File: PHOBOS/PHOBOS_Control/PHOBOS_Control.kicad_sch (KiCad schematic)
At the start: 80 parts, among them J1 Screw_Terminal_01x02, J2 Conn_01x06, J3 Conn_Coaxial, J5 DE9_Pins_MountingHoles, J6 USB4056-03-A_REVA2, SW4 KMR211GLFS, U1 SX1280IMLTRT, U2 TLV9351IDCKR, U3 W25Q128JVSIQ, U4 NCP1117-3.3_SOT223, U5 RP2040, U6 TLV9351IDCKR, U7 TLV9351IDCKR, U8 TLV9351IDCKR, Y1 ABM8-272-T3, Y2 C1E-52.000-10-1012-X-M

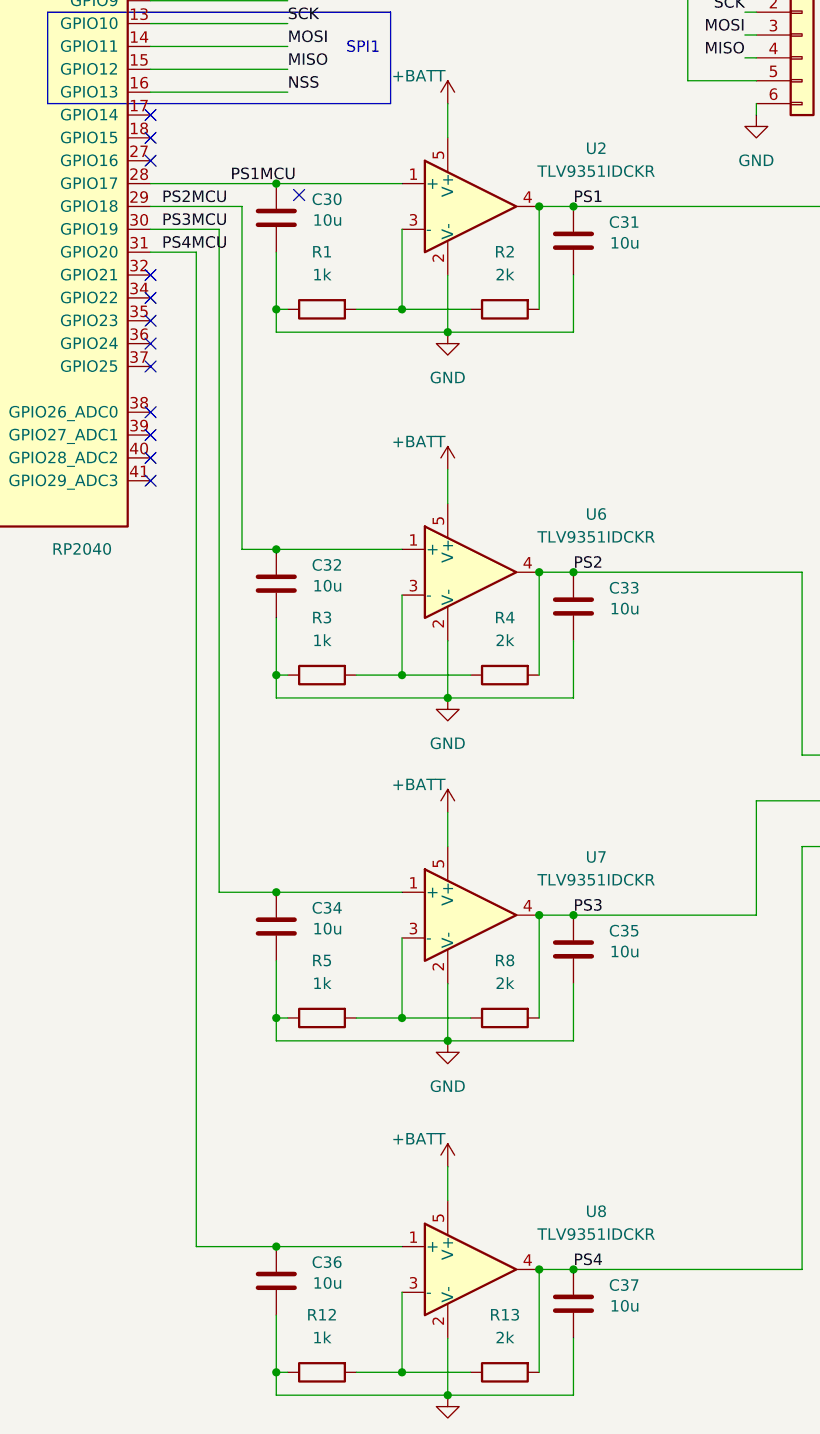
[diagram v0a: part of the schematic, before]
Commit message: some routing added. op amps rearranged
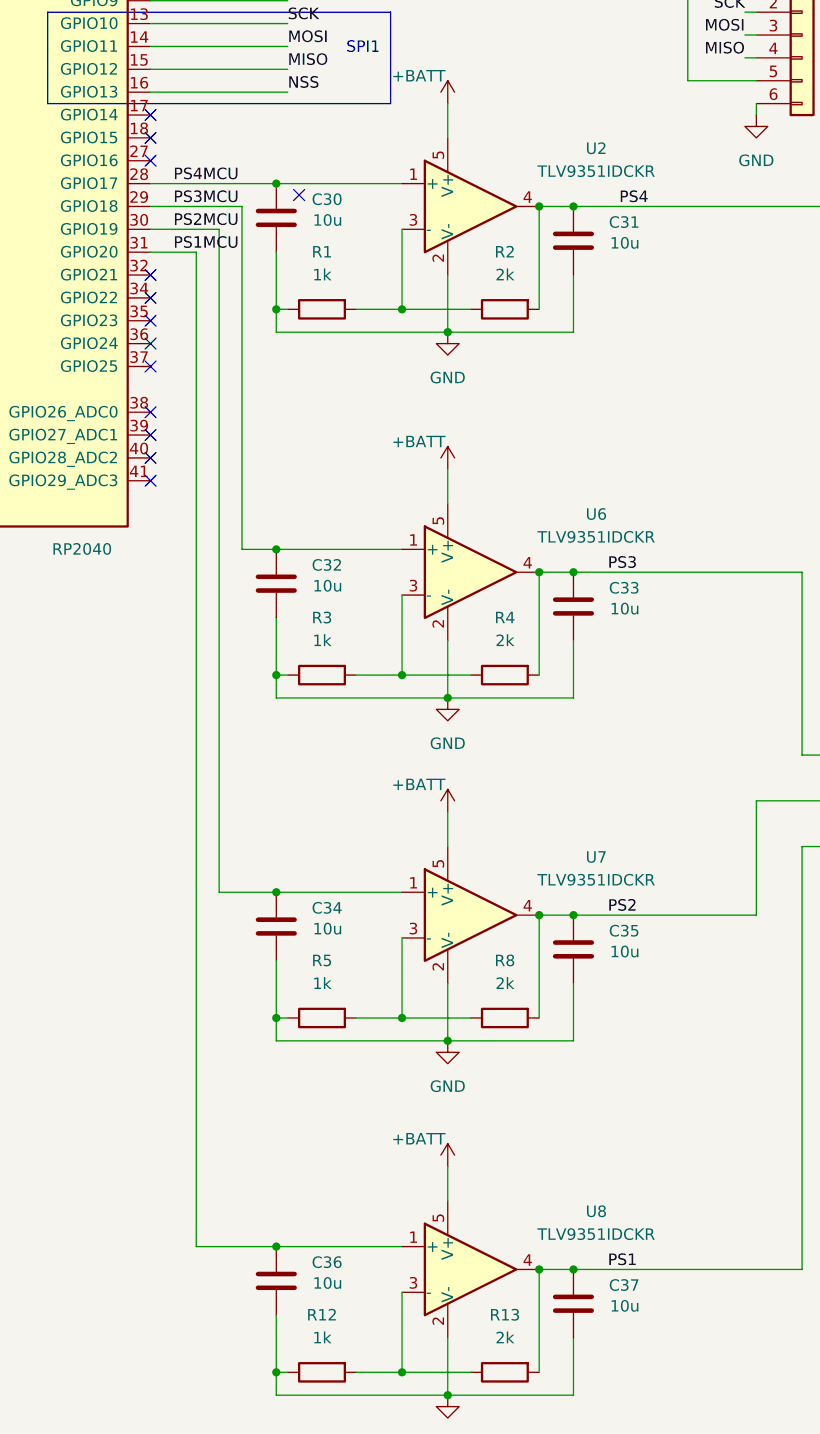
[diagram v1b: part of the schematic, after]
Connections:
- net PS1: now also C37.1, J5.2, R13.2, U8.4; no longer C31.1, J5.5, R2.2, U2.4
- net PS1MCU: now also C36.1, U5.31 (GPIO20), U8.1 (+); no longer C30.1, U2.1 (+), U5.28 (GPIO17)
- net PS2: now also C35.1, J5.3, R8.2, U7.4; no longer C33.1, J5.4, R4.2, U6.4
- net PS2MCU: now also C34.1, U5.30 (GPIO19), U7.1 (+); no longer C32.1, U5.29 (GPIO18), U6.1 (+)
- net PS3: now also C33.1, J5.4, R4.2, U6.4; no longer C35.1, J5.3, R8.2, U7.4
- net PS3MCU: now also C32.1, U5.29 (GPIO18), U6.1 (+); no longer C34.1, U5.30 (GPIO19), U7.1 (+)
- net PS4: now also C31.1, J5.5, R2.2, U2.4; no longer C37.1, J5.2, R13.2, U8.4
- net PS4MCU: now also C30.1, U2.1 (+), U5.28 (GPIO17); no longer C36.1, U5.31 (GPIO20), U8.1 (+)
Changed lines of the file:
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@@
-		)
-	)
-	(label "PS2MCU"
-		(at 320.04 234.95 0)
-		(effects
-			(font
-				(size 1.27 1.27)
-			)
-			(justify left bottom)
-		)
-	)
-	(label "PS1MCU"
-		(at 327.66 232.41 0)
-		(effects
-			(font
-				(size 1.27 1.27)
-			)
-			(justify left bottom)
 		)
 	)
@@
 		)
 	)
-	(label "PS3MCU"
-		(at 320.04 237.49 0)
-		(effects
-			(font
-				(size 1.27 1.27)
-			)
-			(justify left bottom)
-		)
-	)
 	(label "BUSY"
 		(at 472.44 218.44 0)
@@
 		)
 	)
-	(label "PS4MCU"
-		(at 320.04 240.03 0)
-		(effects
-			(font
-				(size 1.27 1.27)
-			)
-			(justify left bottom)
-		)
-	)
 	(label "NSS"
 		(at 426.72 223.52 180)
@@
 		)
 	)
+	(label "PS2MCU"
+		(at 321.31 237.49 0)
+		(effects
+			(font
+				(size 1.27 1.27)
+			)
+			(justify left bottom)
+		)
+	)
 	(label "QSPI_SCLK"
 		(at 241.3 205.74 0)
@@
 		)
 	)
+	(label "PS4"
+		(at 370.84 234.95 0)
+		(effects
+			(font
+				(size 1.27 1.27)
+			)
+			(justify left bottom)
+		)
+	)
 	(label "QSPI_SCLK"
 		(at 162.56 191.77 180)
@@
 		)
 	)
+	(label "PS3"
+		(at 369.57 275.59 0)
+		(effects
+			(font
+				(size 1.27 1.27)
+			)
+			(justify left bottom)
+		)
+	)
 	(label "USB_-"
 		(at 327.66 181.61 180)
@@
 		)
 	)
+	(label "PS1MCU"
+		(at 321.31 240.03 0)
+		(effects
+			(font
+				(size 1.27 1.27)
+			)
+			(justify left bottom)
+		)
+	)
 	(label "DCC_FB"
 		(at 469.9 210.82 0)
@@
 		)
 	)
-	(label "PS2"
-		(at 365.76 275.59 0)
+	(label "PS3MCU"
+		(at 321.31 234.95 0)
 		(effects
 			(font
@@
 		)
 	)
-	(label "PS4"
-		(at 365.76 353.06 0)
-		(effects
-			(font
-				(size 1.27 1.27)
-			)
-			(justify left bottom)
-		)
-	)
 	(label "USB_D+"
 		(at 149.86 119.38 0)
@@
 		)
 	)
+	(label "PS1"
+		(at 369.57 353.06 0)
+		(effects
+			(font
+				(size 1.27 1.27)
+			)
+			(justify left bottom)
+		)
+	)
 	(label "SDA"
 		(at 334.01 199.39 0)
@@
 		)
 	)
+	(label "PS4MCU"
+		(at 321.31 232.41 0)
+		(effects
+			(font
+				(size 1.27 1.27)
+			)
+			(justify left bottom)
+		)
+	)
 	(label "USB_D-"
 		(at 351.79 181.61 180)
@@
 		)
 	)
-	(label "PS1"
-		(at 365.76 234.95 0)
-		(effects
-			(font
-				(size 1.27 1.27)
-			)
-			(justify left bottom)
-		)
-	)
 	(label "SWCLK"
 		(at 241.3 254 0)
@@
 		)
 	)
-	(label "PS3"
-		(at 365.76 313.69 0)
-		(effects
-			(font
-				(size 1.27 1.27)
-			)
-			(justify left bottom)
-		)
-	)
 	(label "SCK"
 		(at 426.72 220.98 180)
@@
 			)
 			(justify right bottom)
+		)
+	)
+	(label "PS2"
+		(at 369.57 313.69 0)
+		(effects
+			(font
+				(size 1.27 1.27)
+			)
+			(justify left bottom)
 		)
 	)
@@
 			(justify left bottom)
 		)
-		(property "Net Class" "PWR"
+		(property "Netclass" "PWR"
 			(at 183.5785 101.6 0)
 			(show_name no)
@@
 			(justify left bottom)
 		)
-		(property "Net Class" "RF"
+		(property "Netclass" "RF"
 			(at 537.9085 231.14 0)
 			(show_name no)
@@
 			(justify left bottom)
 		)
-		(property "Net Class" "RF"
+		(property "Netclass" "RF"
 			(at 525.86 231.14 0)
 			(show_name no)
@@
 			(justify left bottom)
 		)
-		(property "Net Class" "RF"
+		(property "Netclass" "RF"
 			(at 484.5685 231.14 0)
 			(show_name no)
@@
 			(justify left bottom)
 		)
-		(property "Net Class" "RF"
+		(property "Netclass" "RF"
 			(at 508.6985 231.14 0)
 			(show_name no)
@@
 			(justify left bottom)
 		)
-		(property "Net Class" "PWR"
+		(property "Netclass" "PWR"
 			(at 165.7985 101.6 0)
 			(show_name no)

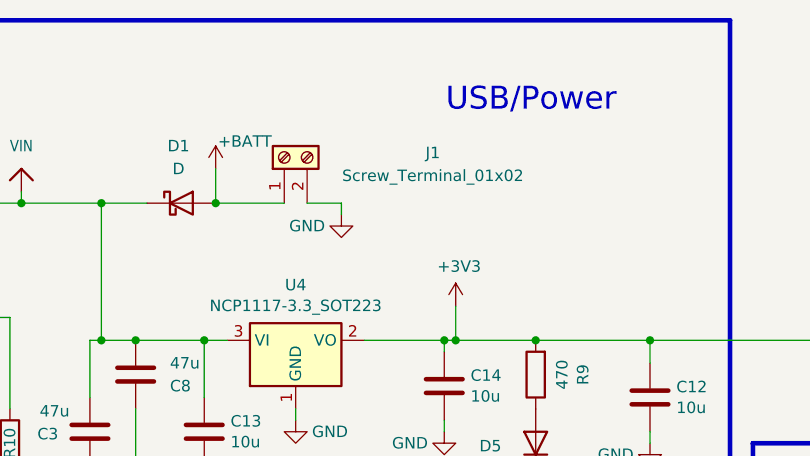
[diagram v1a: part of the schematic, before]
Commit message: USB Routed, routing updated
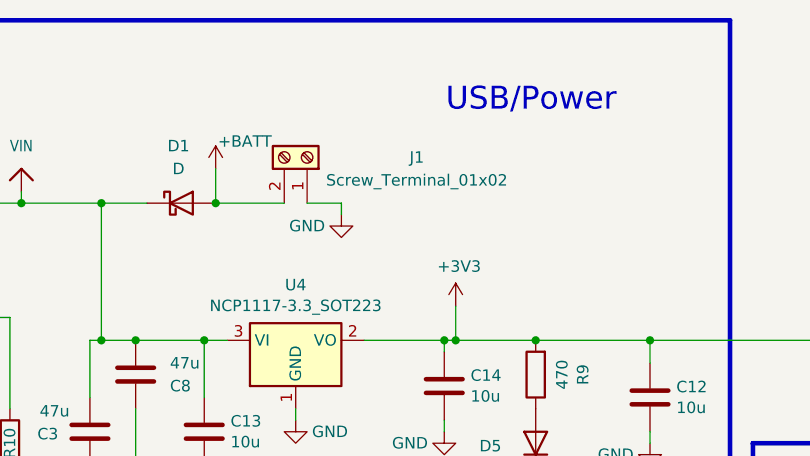
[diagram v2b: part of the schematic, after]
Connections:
- net +BATT: now also J1.2 (Pin_2); no longer J1.1 (Pin_1)
- net GND: now also J1.1 (Pin_1); no longer J1.2 (Pin_2)
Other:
- moved on the sheet: J1
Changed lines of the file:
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@@
 	)
 	(junction
+		(at 181.61 104.14)
+		(diameter 0)
+		(color 0 0 0 0)
+	)
+	(junction
 		(at 332.74 232.41)
 		(diameter 0)
@@
 	)
 	(junction
-		(at 181.61 104.14)
-		(diameter 0)
-		(color 0 0 0 0)
-	)
-	(junction
 		(at 485.14 213.36)
 		(diameter 0)
@@
 			(justify left bottom)
 		)
-		(property "Netclass" "PWR"
+		(property "Net Class" "PWR"
 			(at 183.5785 101.6 0)
 			(show_name no)
@@
 			(justify left bottom)
 		)
-		(property "Netclass" "RF"
+		(property "Net Class" "RF"
 			(at 537.9085 231.14 0)
 			(show_name no)
@@
 			(justify left bottom)
 		)
-		(property "Netclass" "RF"
+		(property "Net Class" "RF"
 			(at 525.86 231.14 0)
 			(show_name no)
@@
 			(justify left bottom)
 		)
-		(property "Netclass" "RF"
+		(property "Net Class" "RF"
 			(at 484.5685 231.14 0)
 			(show_name no)
@@
 			(justify left bottom)
 		)
-		(property "Netclass" "RF"
+		(property "Net Class" "RF"
 			(at 508.6985 231.14 0)
 			(show_name no)
@@
 			(justify left bottom)
 		)
-		(property "Netclass" "PWR"
+		(property "Net Class" "PWR"
 			(at 165.7985 101.6 0)
 			(show_name no)
@@
 	(symbol
 		(lib_id "Connector:Screw_Terminal_01x02")
-		(at 189.23 99.06 90)
+		(at 191.77 99.06 270)
+		(mirror x)
 		(unit 1)
 		(body_style 1)
@@
 		(dnp no)
 		(property "Reference" "J1"
-			(at 205.74 98.552 90)
+			(at 203.962 99.06 90)
 			(show_name no)
 			(do_not_autoplace no)
@@
 		)
 		(property "Value" "Screw_Terminal_01x02"
-			(at 205.74 101.092 90)
+			(at 203.962 101.6 90)
 			(show_name no)
 			(do_not_autoplace no)
@@
 		)
 		(property "Footprint" "TerminalBlock_4Ucon:TerminalBlock_4Ucon_1x02_P3.50mm_Horizontal"
-			(at 189.23 99.06 0)
+			(at 191.77 99.06 0)
 			(hide yes)
 			(show_name no)
@@
 		)
 		(property "Datasheet" ""
-			(at 189.23 99.06 0)
+			(at 191.77 99.06 0)
 			(hide yes)
 			(show_name no)
@@
 		)
 		(property "Description" "Generic screw terminal, single row, 01x02, script generated (kicad-library-utils/schlib/autogen/connector/)"
-			(at 189.23 99.06 0)
+			(at 191.77 99.06 0)
 			(hide yes)
 			(show_name no)
